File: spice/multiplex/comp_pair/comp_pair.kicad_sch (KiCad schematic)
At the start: 10 parts, among them Q1 NMOS, Q2 PMOS

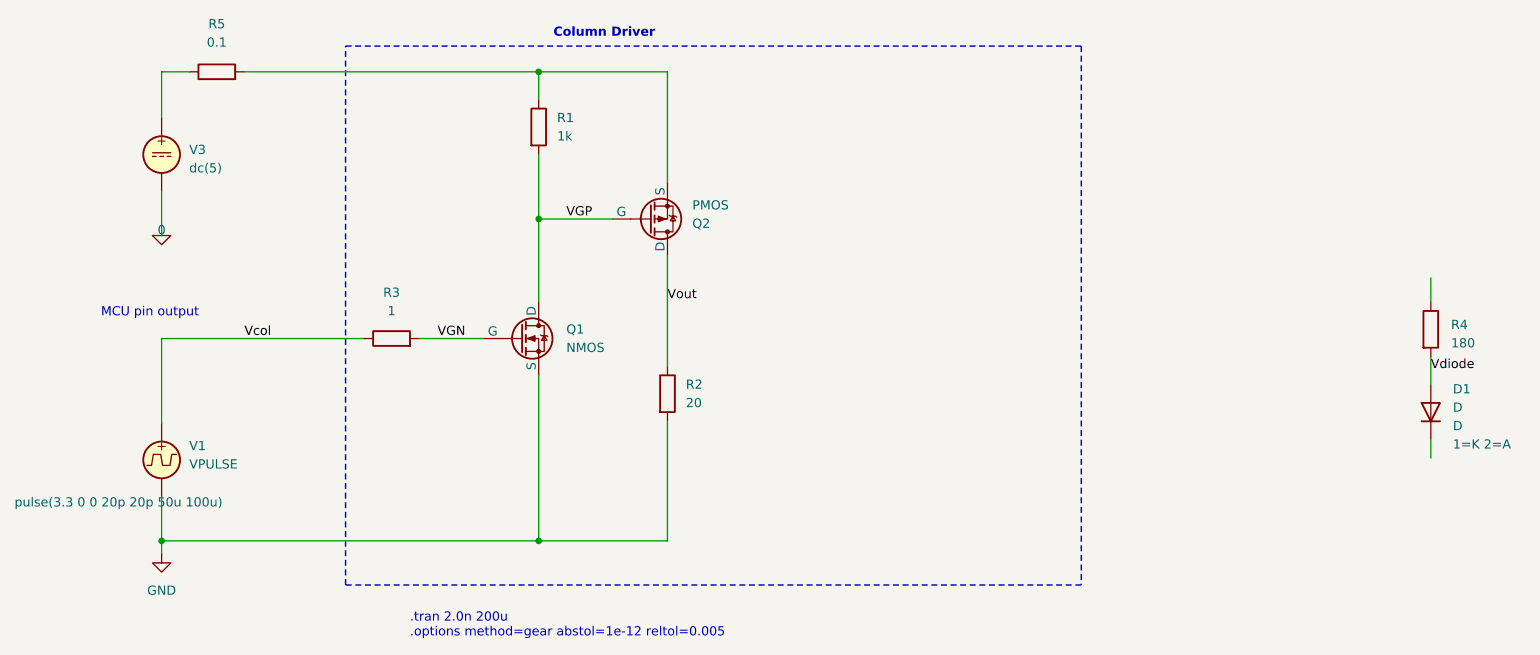
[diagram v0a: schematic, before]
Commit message: Added gate_driver simulation
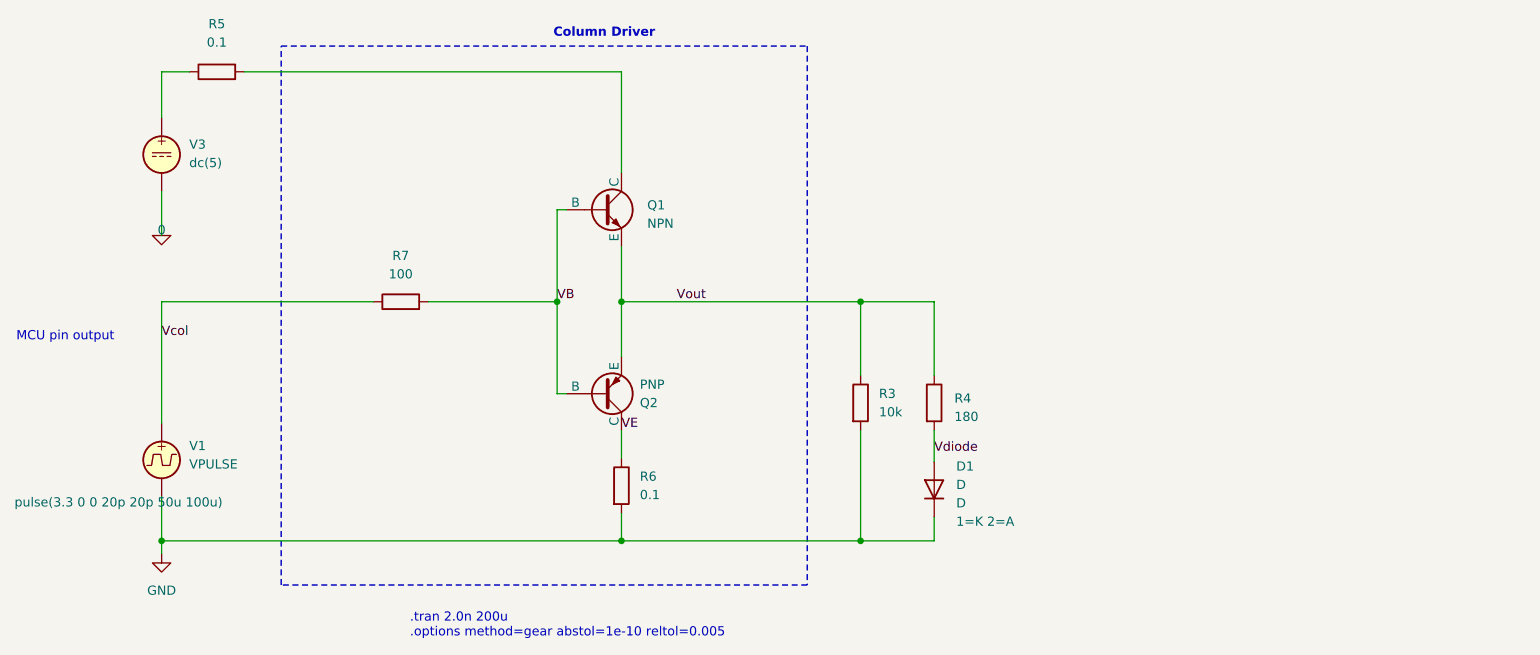
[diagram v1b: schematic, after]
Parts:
- removed Q1: NMOS, symbol Simulation_SPICE:NMOS
- removed Q2: PMOS, symbol Simulation_SPICE:PMOS
- removed R1: 1k, symbol Device:R
- removed R2: 20, symbol Device:R
- added Q1: NPN, symbol Simulation_SPICE:NPN
- added Q2: PNP, symbol Simulation_SPICE:PNP
- added R6: 0.1, symbol Device:R
- added R7: 100, symbol Device:R
- R3: value 1 -> 10k
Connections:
- net VGN is gone; now on net GND: R3.2
- net GND: now also D1.1 (K), R6.2
- net Vcol: now also R7.1; no longer R3.1
- net Vout: now also R3.1, R4.1, Q1.3 (E), Q2.3 (E)
- net at R5.2: now also Q1.1 (C)
- new net VB: Q1.2 (B), Q2.2 (B), R7.2
- new net VE: Q2.1 (C), R6.1
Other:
- note added: ".tran 2.0n 200u .options method=gear abstol=1e-10 reltol=0.005"
- note removed: ".tran 2.0n 200u .options method=gear abstol=1e-12 reltol=0.005"
- moved on the sheet: D1, R4
